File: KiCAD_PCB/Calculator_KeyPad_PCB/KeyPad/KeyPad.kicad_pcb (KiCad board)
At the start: 2 copper layers, 43 parts, among them J1 5034801000, SW1 SW_SPST, SW10 SW_SPST, SW11 SW_SPST, SW12 SW_SPST, SW13 SW_SPST, SW14 SW_SPST, SW15 SW_SPST, SW16 SW_SPST, SW17 SW_SPST, SW18 SW_SPST, SW19 SW_SPST, SW2 SW_SPST, SW20 SW_SPST, SW21 SW_SPST, SW3 SW_SPST, SW4 SW_SPST, SW5 SW_SPST, SW6 SW_SPST, SW7 SW_SPST, SW8 SW_SPST, SW9 SW_SPST

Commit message: NumPad PCB Updates
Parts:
- moved SW10 103.8 mm to (154.7, 88.0), turned to 90 degrees
- moved SW1 93.6 mm to (142.8, 72.0), turned to 90 degrees
- moved SW15 90.4 mm to (166.6, 72.0), turned to 90 degrees
- moved SW16 88.3 mm to (166.6, 80.0), turned to 90 degrees
- moved SW3 81.2 mm to (142.8, 88.0), turned to 90 degrees
- moved SW2 75.0 mm to (142.8, 80.0), turned to 90 degrees
- moved SW17 71.7 mm to (166.6, 88.0), turned to 90 degrees
- moved SW9 61.8 mm to (154.7, 80.0), turned to 90 degrees
- moved SW8 49.8 mm to (154.7, 72.0), turned to 90 degrees

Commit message: Updated NumPad PCB
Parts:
- moved SW20 120.6 mm to (166.6, 112.0), turned to 90 degrees
- moved SW21 113.7 mm to (166.6, 120.0), turned to 90 degrees
- moved SW13 110.6 mm to (154.7, 112.0), turned to 90 degrees
- moved SW5 103.2 mm to (142.8, 104.0), turned to 90 degrees
- moved SW6 101.0 mm to (142.8, 112.0), turned to 90 degrees
- moved SW19 95.6 mm to (166.6, 104.0), turned to 90 degrees
- moved SW12 90.8 mm to (154.7, 104.0), turned to 90 degrees
- moved SW18 88.2 mm to (166.6, 96.0), turned to 90 degrees
- moved SW14 86.3 mm to (154.7, 120.0), turned to 90 degrees
- moved SW7 84.4 mm to (142.8, 120.0), turned to 90 degrees
- moved SW11 76.5 mm to (154.7, 96.0), turned to 90 degrees
- moved SW4 54.5 mm to (142.8, 96.0), turned to 90 degrees

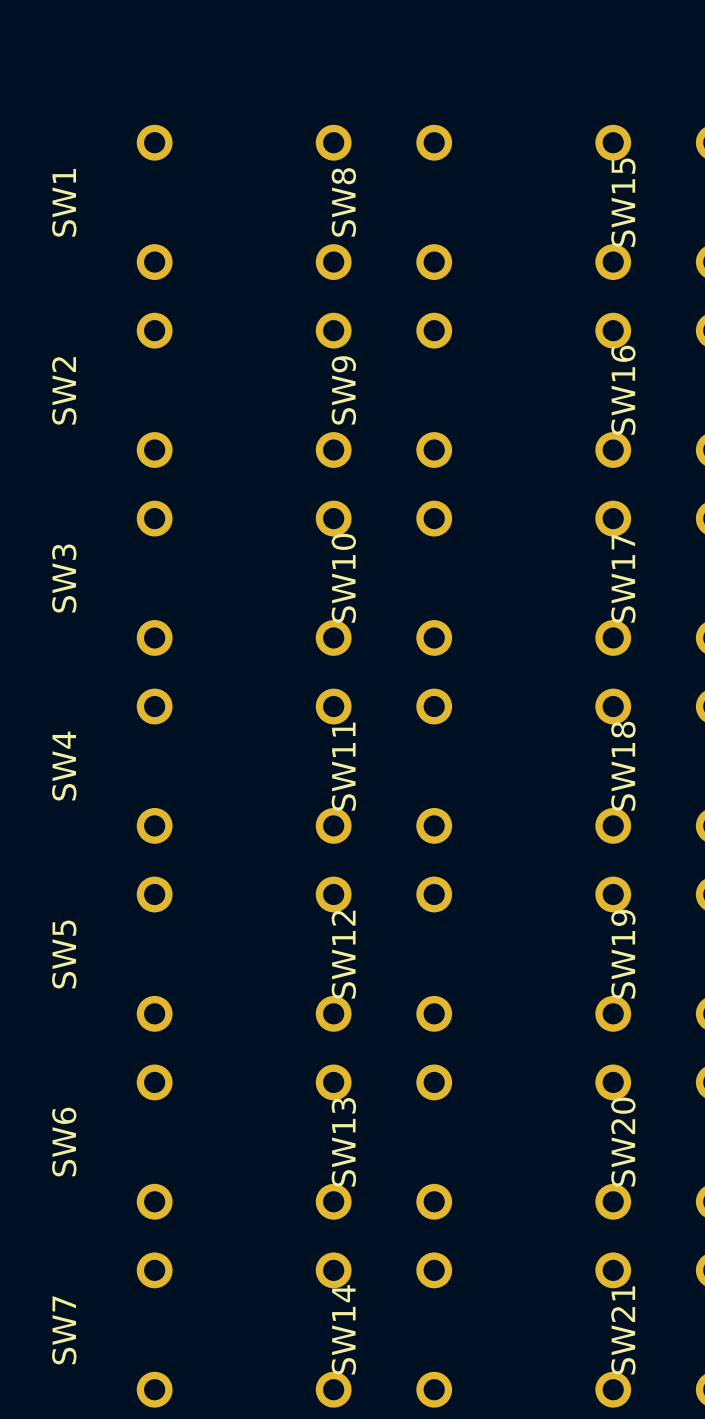
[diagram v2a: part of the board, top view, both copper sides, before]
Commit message: PCB NumPad Updates
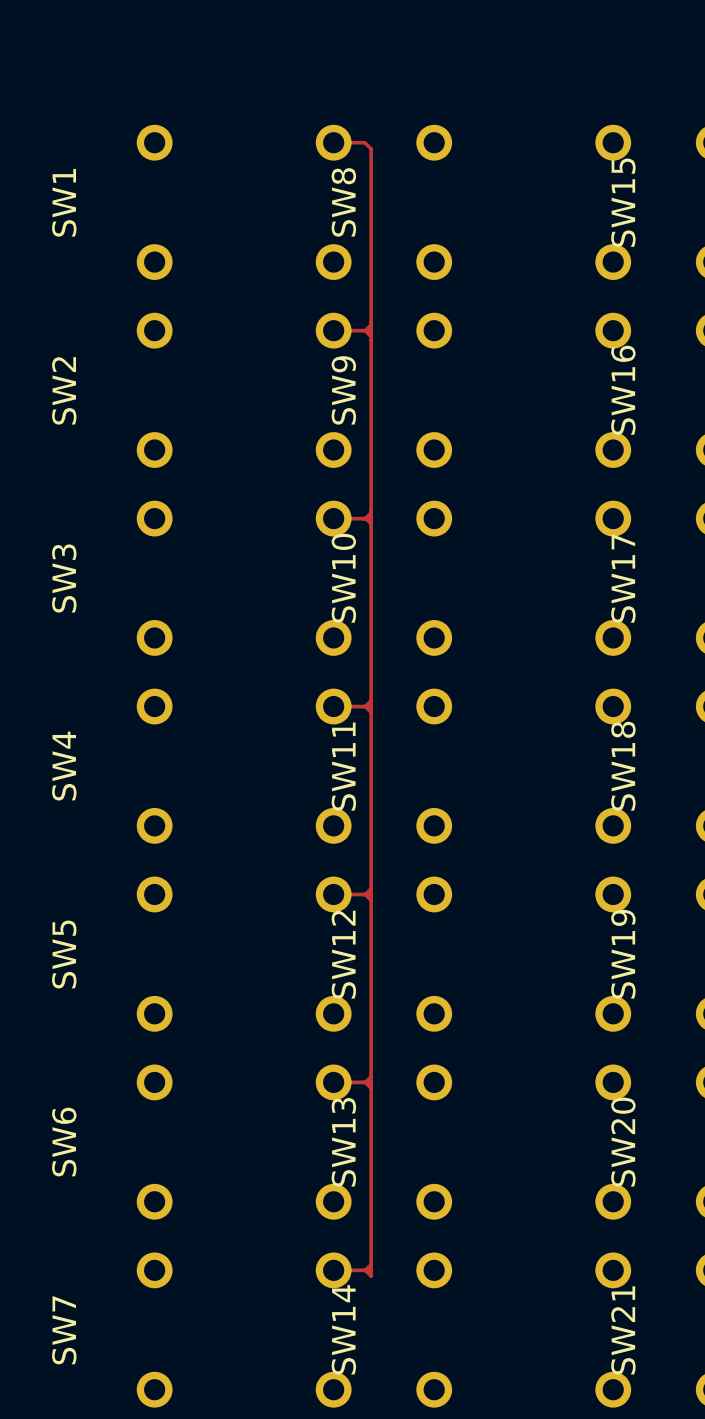
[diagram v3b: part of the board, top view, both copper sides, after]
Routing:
- net /Col13: track 0.00 -> 63.3 mm
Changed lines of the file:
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@@
       (net 30 "/Col15") (pinfunction "B") (pintype "passive"))
   )
-  (gr_line (start 60.130024 79.787965) (end 24.130024 79.787965) (layer "Dwgs.User") (width 0.2))
-  (gr_circle (center 24.130024 81.787965) (end 25.130024 81.787965) (layer "Dwgs.User") (width 0.2) (fill none))
-  (gr_arc (start 22.130024 81.787965) (mid 22.715824 80.373783) (end 24.130024 79.787965) (layer "Dwgs.User") (width 0.2))
-  (gr_line (start 22.130024 81.787965) (end 22.130024 137.787965) (layer "Dwgs.User") (width 0.2))
-  (gr_circle (center 60.130024 81.787965) (end 61.130024 81.787965) (layer "Dwgs.User") (width 0.2) (fill none))
-  (gr_arc (start 62.130024 137.787965) (mid 61.544251 139.20221) (end 60.130024 139.787965) (layer "Dwgs.User") (width 0.2))
-  (gr_line (start 24.130024 139.787965) (end 60.130024 139.787965) (layer "Dwgs.User") (width 0.2))
-  (gr_arc (start 60.130024 79.787965) (mid 61.544234 80.373758) (end 62.130024 81.787965) (layer "Dwgs.User") (width 0.2))
-  (gr_arc (start 24.130024 139.787965) (mid 22.715807 139.202185) (end 22.130024 137.787965) (layer "Dwgs.User") (width 0.2))
-  (gr_circle (center 24.130024 137.787965) (end 25.130024 137.787965) (layer "Dwgs.User") (width 0.2) (fill none))
-  (gr_line (start 62.130024 137.787965) (end 62.130024 81.787965) (layer "Dwgs.User") (width 0.2))
-  (gr_circle (center 60.130024 137.787965) (end 61.130024 137.787965) (layer "Dwgs.User") (width 0.2) (fill none))
+  (gr_line (start 63.45 86) (end 27.45 86) (layer "Dwgs.User") (width 0.2))
+  (gr_circle (center 27.45 88) (end 28.45 88) (layer "Dwgs.User") (width 0.2) (fill none))
+  (gr_arc (start 25.45 88) (mid 26.0358 86.585818) (end 27.45 86) (layer "Dwgs.User") (width 0.2))
+  (gr_line (start 25.45 88) (end 25.45 144) (layer "Dwgs.User") (width 0.2))
+  (gr_circle (center 63.45 88) (end 64.45 88) (layer "Dwgs.User") (width 0.2) (fill none))
+  (gr_arc (start 65.45 144) (mid 64.864227 145.414245) (end 63.45 146) (layer "Dwgs.User") (width 0.2))
+  (gr_line (start 27.45 146) (end 63.45 146) (layer "Dwgs.User") (width 0.2))
+  (gr_arc (start 63.45 86) (mid 64.86421 86.585793) (end 65.45 88) (layer "Dwgs.User") (width 0.2))
+  (gr_arc (start 27.45 146) (mid 26.035783 145.41422) (end 25.45 144) (layer "Dwgs.User") (width 0.2))
+  (gr_circle (center 27.45 144) (end 28.45 144) (layer "Dwgs.User") (width 0.2) (fill none))
+  (gr_line (start 65.45 144) (end 65.45 88) (layer "Dwgs.User") (width 0.2))
+  (gr_circle (center 63.45 144) (end 64.45 144) (layer "Dwgs.User") (width 0.2) (fill none))
+  (segment (start 148.204 93.216) (end 148.204 85.676) (width 0.15) (layer "F.Cu") (net 29))
+  (segment (start 148.204 109.475) (end 148.204 109.216) (width 0.15) (layer "F.Cu") (net 29))
+  (segment (start 148.204 85.676) (end 148.204 85.4252) (width 0.15) (layer "F.Cu") (net 29))
+  (segment (start 148.204 77.216) (end 148.204 77.094) (width 0.15) (layer "F.Cu") (net 29))
+  (segment (start 147.8898 85.46) (end 147.96 85.46) (width 0.15) (layer "F.Cu") (net 29))
+  (segment (start 147.96 93.462) (end 148.204 93.706) (width 0.15) (layer "F.Cu") (net 29))
+  (segment (start 148.204 109.216) (end 148.204 101.706) (width 0.15) (layer "F.Cu") (net 29))
+  (segment (start 148.204 109.706) (end 148.204 109.475) (width 0.15) (layer "F.Cu") (net 29))
+  (segment (start 148.204 93.706) (end 148.204 93.475) (width 0.15) (layer "F.Cu") (net 29))
+  (segment (start 147.96 117.462) (end 148.204 117.706) (width 0.15) (layer "F.Cu") (net 29))
+  (segment (start 147.96 109.46) (end 148.204 109.216) (width 0.15) (layer "F.Cu") (net 29))
+  (segment (start 147.96 93.46) (end 148.204 93.216) (width 0.15) (layer "F.Cu") (net 29))
+  (segment (start 147.988 85.46) (end 148.204 85.676) (width 0.15) (layer "F.Cu") (net 29))
+  (segment (start 147.8634 117.46) (end 148.189 117.46) (width 0.15) (layer "F.Cu") (net 29))
+  (segment (start 148.204 85.216) (end 148.204 85.095) (width 0.15) (layer "F.Cu") (net 29))
+  (segment (start 147.8634 109.46) (end 148.189 109.46) (width 0.15) (layer "F.Cu") (net 29))
+  (segment (start 146.61 85.46) (end 147.8898 85.46) (width 0.15) (layer "F.Cu") (net 29))
+  (segment (start 146.61 101.46) (end 147.8634 101.46) (width 0.15) (layer "F.Cu") (net 29))
+  (segment (start 148.204 77.856) (end 148.204 77.7544) (width 0.15) (layer "F.Cu") (net 29))
+  (segment (start 148.204 85.095) (end 148.204 77.856) (width 0.15) (layer "F.Cu") (net 29))
+  (segment (start 147.96 117.46) (end 148.204 117.216) (width 0.15) (layer "F.Cu") (net 29))
+  (segment (start 148.204 69.728) (end 147.936 69.46) (width 0.15) (layer "F.Cu") (net 29))
+  (segment (start 147.96 77.462) (end 148.204 77.706) (width 0.15) (layer "F.Cu") (net 29))
+  (segment (start 146.61 77.46) (end 147.8634 77.46) (width 0.15) (layer "F.Cu") (net 29))
+  (segment (start 148.204 77.706) (end 148.204 77.475) (width 0.15) (layer "F.Cu") (net 29))
+  (segment (start 148.204 85.4252) (end 148.204 85.216) (width 0.15) (layer "F.Cu") (net 29))
+  (segment (start 147.8634 93.46) (end 148.189 93.46) (width 0.15) (layer "F.Cu") (net 29))
+  (segment (start 147.8634 101.46) (end 148.189 101.46) (width 0.15) (layer "F.Cu") (net 29))
+  (segment (start 148.204 77.094) (end 148.204 69.728) (width 0.15) (layer "F.Cu") (net 29))
+  (segment (start 147.936 69.46) (end 146.61 69.46) (width 0.15) (layer "F.Cu") (net 29))
+  (segment (start 147.8898 85.46) (end 148.1692 85.46) (width 0.15) (layer "F.Cu") (net 29))
+  (segment (start 147.96 101.46) (end 148.204 101.216) (width 0.15) (layer "F.Cu") (net 29))
+  (segment (start 148.204 101.475) (end 148.204 101.216) (width 0.15) (layer "F.Cu") (net 29))
+  (segment (start 148.204 77.475) (end 148.204 77.216) (width 0.15) (layer "F.Cu") (net 29))
+  (segment (start 147.96 109.462) (end 148.204 109.706) (width 0.15) (layer "F.Cu") (net 29))
+  (segment (start 146.61 93.46) (end 147.8634 93.46) (width 0.15) (layer "F.Cu") (net 29))
+  (segment (start 146.61 109.46) (end 147.8634 109.46) (width 0.15) (layer "F.Cu") (net 29))
+  (segment (start 148.204 117.475) (end 148.204 117.216) (width 0.15) (layer "F.Cu") (net 29))
+  (segment (start 147.96 101.462) (end 148.204 101.706) (width 0.15) (layer "F.Cu") (net 29))
+  (segment (start 148.1692 85.46) (end 148.204 85.4252) (width 0.15) (layer "F.Cu") (net 29))
+  (segment (start 147.96 77.46) (end 148.204 77.216) (width 0.15) (layer "F.Cu") (net 29))
+  (segment (start 148.204 93.475) (end 148.204 93.216) (width 0.15) (layer "F.Cu") (net 29))
+  (segment (start 148.204 117.216) (end 148.204 109.706) (width 0.15) (layer "F.Cu") (net 29))
+  (segment (start 148.204 117.706) (end 148.204 117.475) (width 0.15) (layer "F.Cu") (net 29))
+  (segment (start 147.8634 77.46) (end 148.189 77.46) (width 0.15) (layer "F.Cu") (net 29))
+  (segment (start 148.204 101.216) (end 148.204 93.706) (width 0.15) (layer "F.Cu") (net 29))
+  (segment (start 148.204 101.706) (end 148.204 101.475) (width 0.15) (layer "F.Cu") (net 29))
+  (segment (start 146.61 117.46) (end 147.8634 117.46) (width 0.15) (layer "F.Cu") (net 29))
+  (segment (start 147.96 85.46) (end 148.204 85.216) (width 0.15) (layer "F.Cu") (net 29))
   (group "" (id 70b3744a-5195-4f78-a589-c73ffc35d77c)
     (members

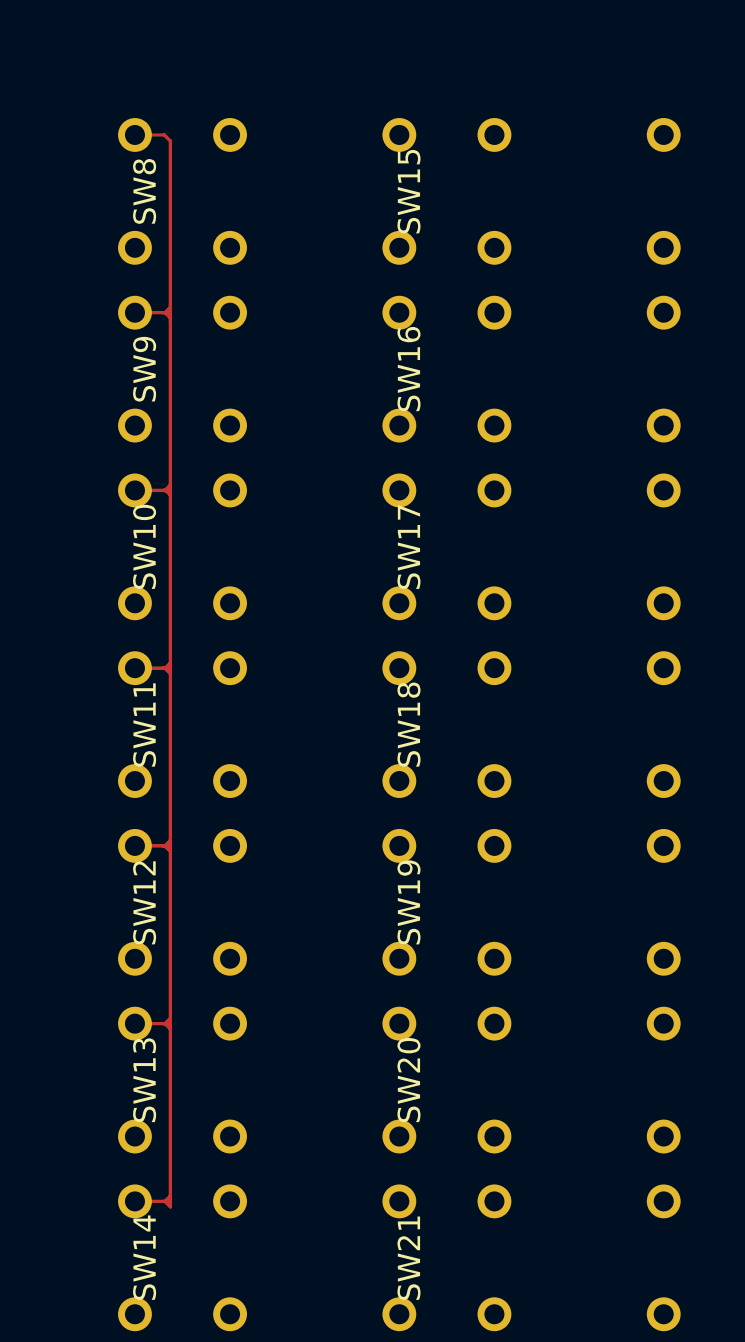
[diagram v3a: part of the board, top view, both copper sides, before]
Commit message: PCB NumPad Updates
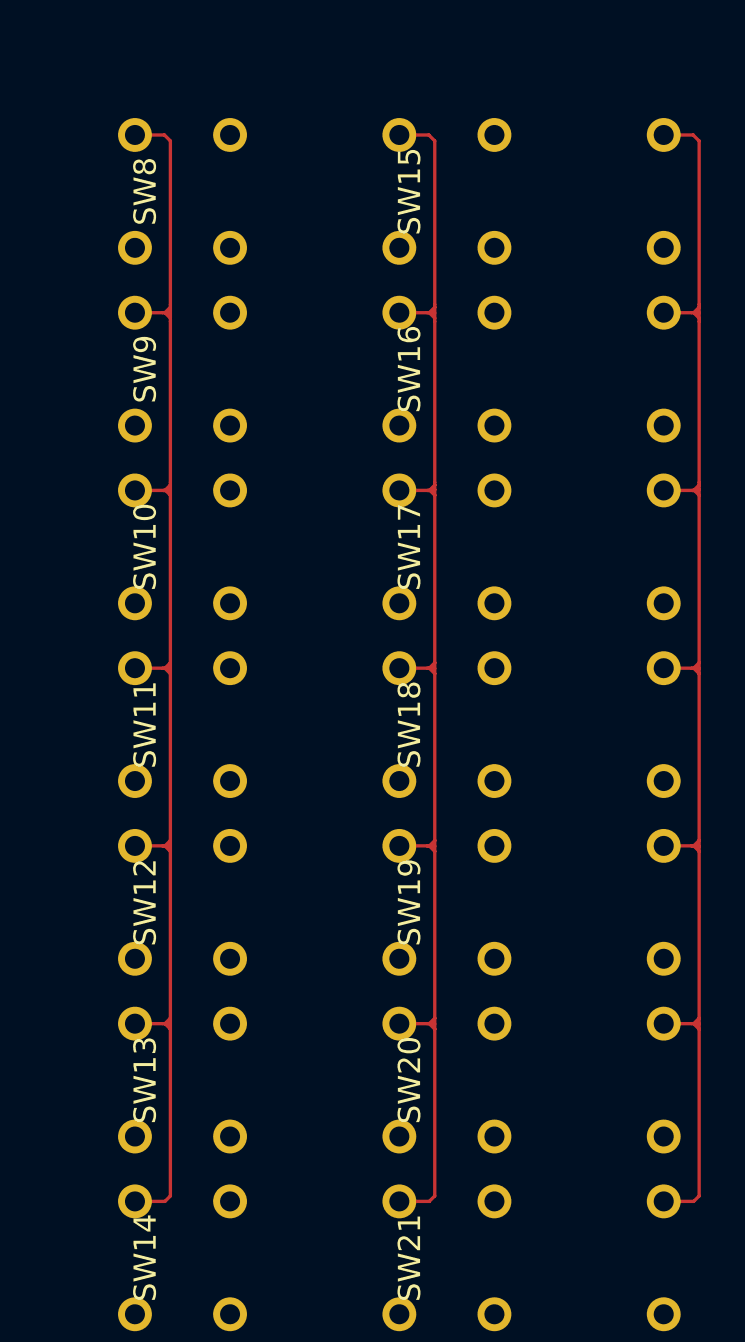
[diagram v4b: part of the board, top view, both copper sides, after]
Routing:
- net /Col14: track 0.00 -> 62.2 mm
- net /Col15: track 0.00 -> 62.2 mm
- net /Col13: track 63.3 -> 62.2 mm

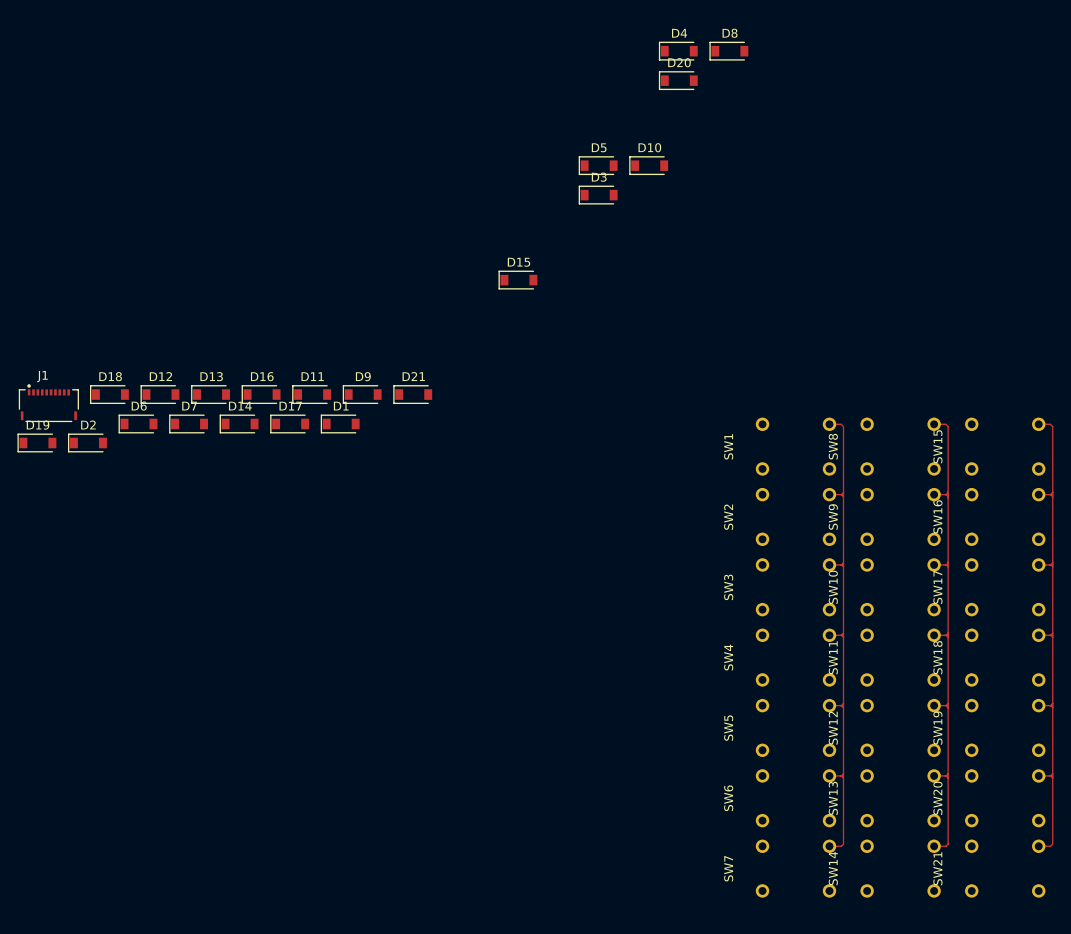
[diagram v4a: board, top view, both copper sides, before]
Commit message: PCB NumPad Updates
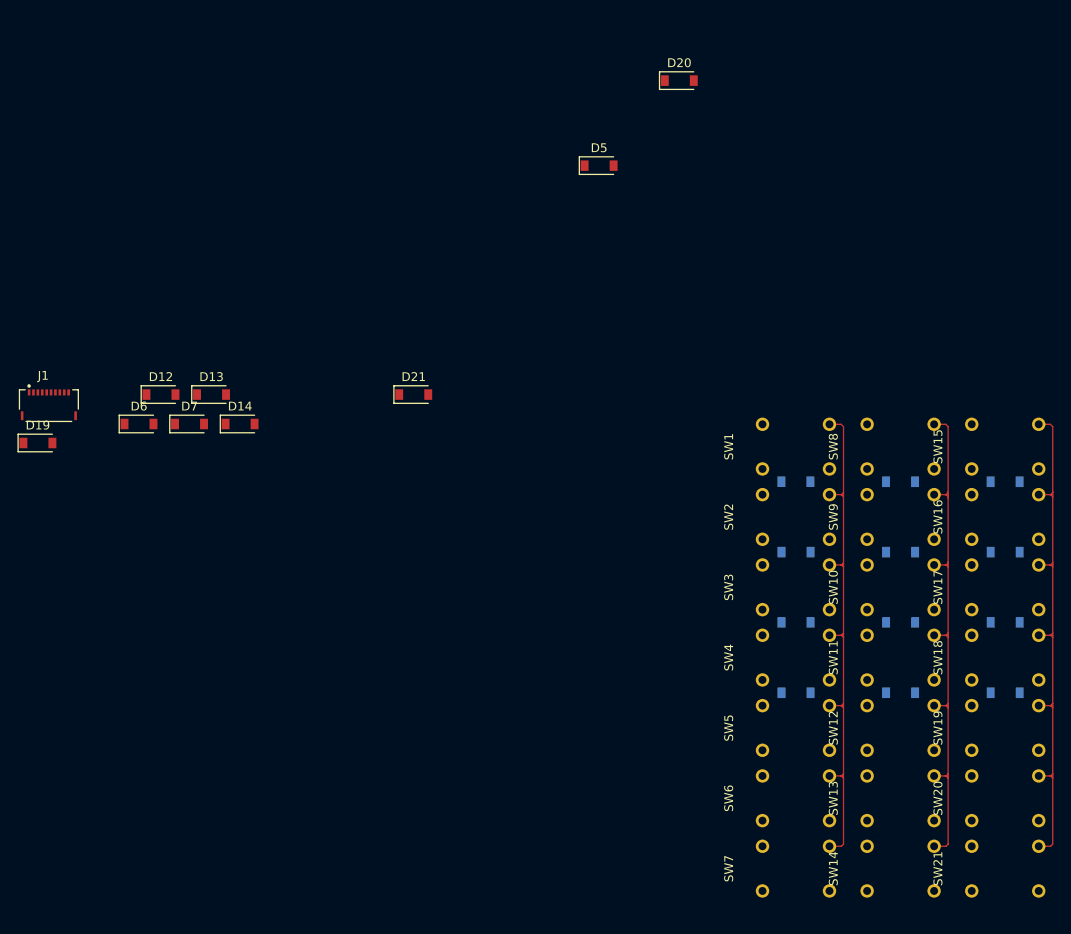
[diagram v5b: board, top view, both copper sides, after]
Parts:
- D1, D10, D11, D15, D16, D17, D18, D2, D3, D4, D8, D9: moved to B.Cu
- moved D18 107.3 mm to (166.6, 100.0)
- moved D16 86.4 mm to (166.6, 84.0)
- moved D17 84.4 mm to (166.6, 92.0)
- moved D2 81.4 mm to (142.8, 84.0)
- moved D11 75.0 mm to (154.7, 100.0)
- moved D4 74.2 mm to (142.8, 100.0)
- moved D9 63.7 mm to (154.7, 84.0)
- moved D15 59.9 mm to (166.6, 76.0)
- moved D10 59.3 mm to (154.7, 92.0)
- moved D3 53.5 mm to (142.8, 92.0)
- moved D8 52.7 mm to (154.7, 76.0)
- moved D1 52.1 mm to (142.8, 76.0)
